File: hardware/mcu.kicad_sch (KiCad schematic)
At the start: 25 parts, among them J1 Micro_SD_Card, SW8 BOOT, U1 ESP32-S3-WROOM-1, U10 PCA9555PW, U8 Ai-Thinker-Ra-02

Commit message: Cleanup project library
Add hexpansion connector symbol, footprint and 3d
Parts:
- FID1: footprint lib:display -> badge:display
- MK1: footprint lib:microfono -> badge:microfono; symbol microphone_crystal:Microphone_Crystal -> badge:Microphone_Crystal
- RV1: footprint lib:JOYSTICK_ANALOG_MINITHM -> badge:JOYSTICK_ANALOG_MINITHM
- SW8: footprint lib:bottonepiccolo_C2888430 -> badge:bottonepiccolo_C2888430
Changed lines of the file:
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@@
 			)
 		)
-		(property "Footprint" "lib:display"
+		(property "Footprint" "badge:display"
 			(at 185.42 55.88 0)
 			(effects
@@
 	)
 	(symbol
-		(lib_id "microphone_crystal:Microphone_Crystal")
+		(lib_id "badge:Microphone_Crystal")
 		(at 35.56 157.48 0)
 		(unit 1)
@@
 			)
 		)
-		(property "Footprint" "lib:microfono"
+		(property "Footprint" "badge:microfono"
 			(at 31.75 159.258 90)
 			(effects
@@
 			)
 		)
-		(property "Footprint" "lib:bottonepiccolo_C2888430"
+		(property "Footprint" "badge:bottonepiccolo_C2888430"
 			(at 41.91 55.88 0)
 			(effects
@@
 			)
 		)
-		(property "Footprint" "lib:JOYSTICK_ANALOG_MINITHM"
+		(property "Footprint" "badge:JOYSTICK_ANALOG_MINITHM"
 			(at 252.73 78.74 0)
 			(effects
@@
 			)
 		)
-		(property "Footprint" "lib:JOYSTICK_ANALOG_MINITHM"
+		(property "Footprint" "badge:JOYSTICK_ANALOG_MINITHM"
 			(at 267.97 92.71 0)
 			(effects

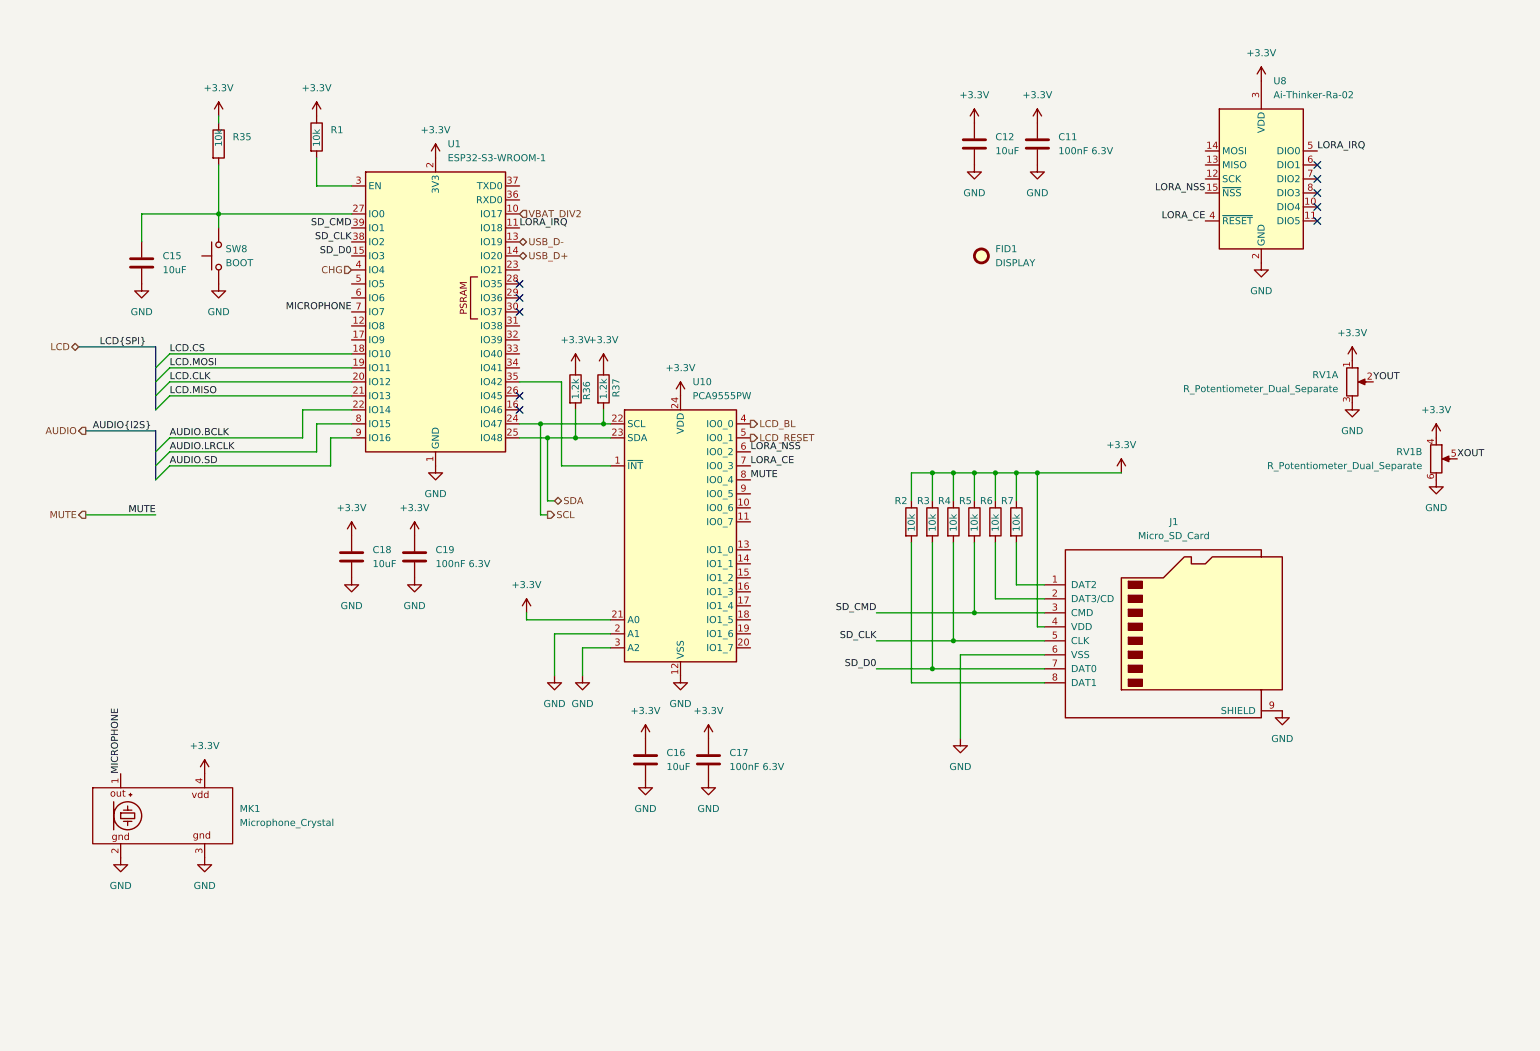
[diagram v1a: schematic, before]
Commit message: Add sdcard fooprint
Remove io expander
Reorganize a bit the mcu schematic
Routed audio
Routed lora
Partial pin swapping of esp32 for facilitating routing
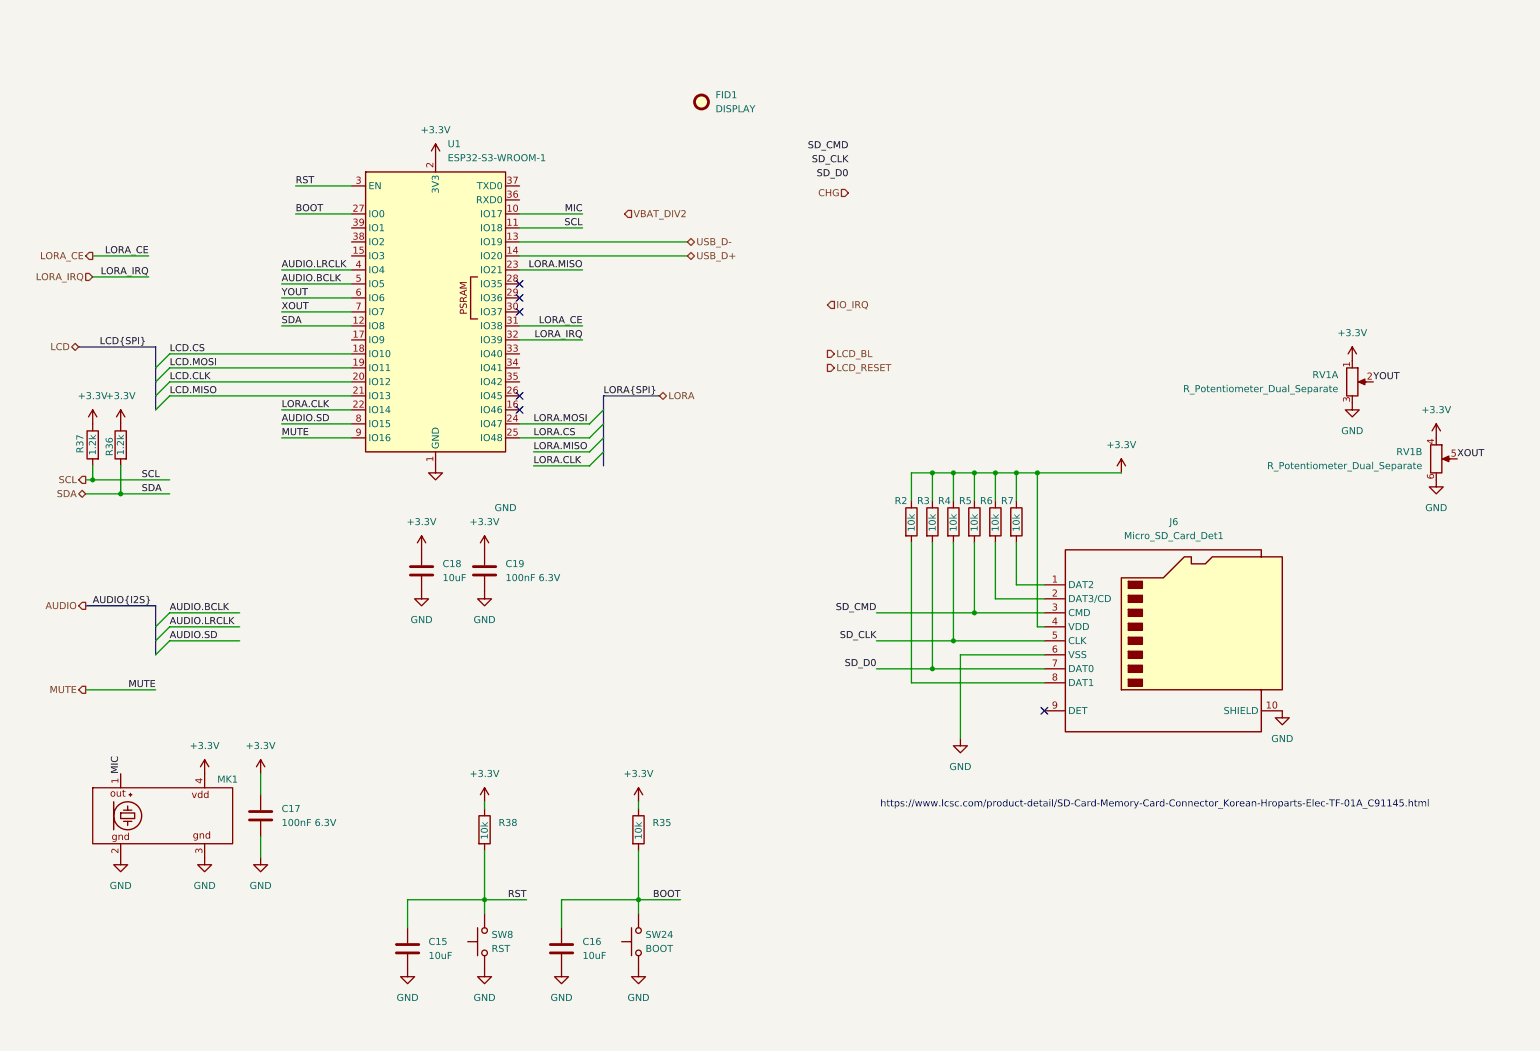
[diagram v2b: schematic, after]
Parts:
- removed C11: 100nF 6.3V, Capacitor_SMD:C_0402_1005Metric, symbol Device:C
- removed C12: 10uF, Capacitor_SMD:C_0603_1608Metric, symbol Device:C
- removed J1: Micro_SD_Card, Connector_Card:microSD_HC_Hirose_DM3D-SF, symbol Connector:Micro_SD_Card
- removed R1: 10k, Resistor_SMD:R_0603_1608Metric, symbol Device:R
- removed U10: PCA9555PW, Package_SO:TSSOP-24_4.4x7.8mm_P0.65mm, symbol Interface_Expansion:PCA9555PW
- removed U8: Ai-Thinker-Ra-02, RF_Module:Ai-Thinker-Ra-01-LoRa, symbol RF_Module:Ai-Thinker-Ra-02
- added J6: Micro_SD_Card_Det1, badge:TF-01A, symbol Connector:Micro_SD_Card_Det1
- added R38: 10k, Resistor_SMD:R_0603_1608Metric, symbol Device:R
- added SW24: BOOT, badge:bottonepiccolo_C2888430, symbol Switch:SW_Push
- SW8: value BOOT -> RST
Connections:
- net +3.3V: now also J6.4 (VDD), R38.1; no longer C16.1
- net AUDIO.BCLK: now also U1.5 (IO5); no longer U1.22 (IO14)
- net AUDIO.LRCLK: now also U1.4 (IO4); no longer U1.8 (IO15)
- net AUDIO.SD: now also U1.8 (IO15); no longer U1.9 (IO16)
- net CHG: no longer U1.4 (IO4)
- net GND: now also J6.10 (SHIELD), J6.6 (VSS), SW24.1
- net LORA_CE: now also U1.31 (IO38)
- net LORA_IRQ: now also U1.32 (IO39); no longer U1.11 (IO18)
- net MUTE: now also U1.9 (IO16)
- net SCL: now also U1.11 (IO18); no longer U1.24 (IO47)
- net SDA: now also U1.12 (IO8); no longer U1.25 (IO48)
- net SD_CLK: now also J6.5 (CLK); no longer U1.38 (IO2)
- net SD_CMD: now also J6.3 (CMD); no longer U1.39 (IO1)
- net SD_D0: now also J6.7 (DAT0); no longer U1.15 (IO3)
- net VBAT_DIV2: no longer U1.10 (IO17)
- net XOUT: now also U1.7 (IO7)
- net YOUT: now also U1.6 (IO6)
- net at R2.2: now also J6.8 (DAT1)
- net BOOT: now reaches R35.2, U1.27 (IO0)
- net BOOT: now also C16.1, SW24.2; no longer C15.1, SW8.2
- net LORA.MISO: now reaches U1.23 (IO21)
- net RST: now reaches U1.3 (EN)
- net RST: now also C15.1, SW8.2, R38.2
- net at R7.2: now also J6.1 (DAT2)
- net at R6.2: now also J6.2 (DAT3/CD)
- net MICROPHONE renamed MIC
- net MIC: now also U1.10 (IO17); no longer U1.7 (IO7)
- new net LORA.CLK: U1.22 (IO14)
- new net LORA.CS: U1.25 (IO48)
- new net LORA.MOSI: U1.24 (IO47)
- no-connect marks 10 -> 6
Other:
- note added: "https://www.lcsc.com/product-detail/SD-Card-Memory-Card-Connector_Korean-Hroparts-Elec-TF-01A_C91145.html"
- moved on the sheet: C18, C19, FID1

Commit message: Route all board
Fix CS missing for SD card
Add IMU symbol and footprint to the project lib
Finish esp32 pinswaps
Move non critical signals to the keyboard IO expander
Add power flag symbols
Fix Dpad pin type
Fix IMU pin type
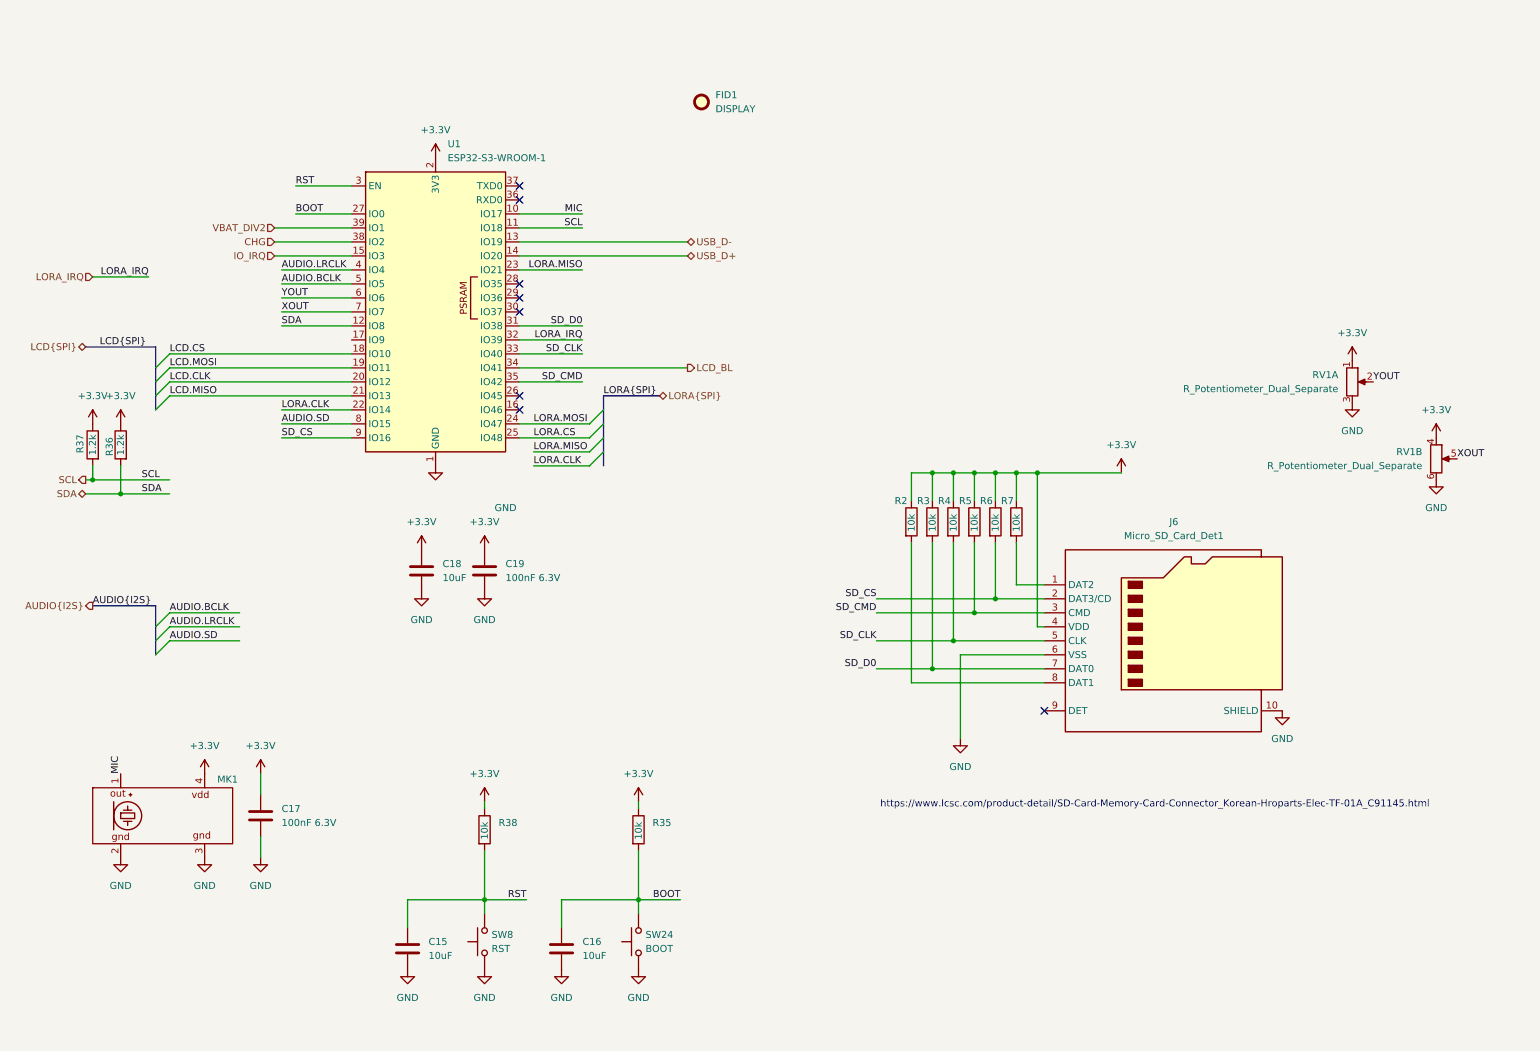
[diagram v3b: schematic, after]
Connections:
- net LORA_CE is gone; now on net SD_D0: U1.31 (IO38)
- net MUTE is gone; now on net SD_CS: U1.9 (IO16)
- net CHG: now also U1.38 (IO2)
- net IO_IRQ: now also U1.15 (IO3)
- net LCD_BL: now also U1.34 (IO41)
- net SD_CLK: now also U1.33 (IO40)
- net SD_CMD: now also U1.35 (IO42)
- net VBAT_DIV2: now also U1.39 (IO1)
- net SD_CS: now reaches J6.2 (DAT3/CD), R6.2
- no-connect marks 6 -> 8
